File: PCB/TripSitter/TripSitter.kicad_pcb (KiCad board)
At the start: 4 copper layers, 203 x 85 mm, 155 parts, among them IC1 MT25QL256ABA1EW9-0SIT, IC701 IP4220CZ6, J1 Conn_ARM_JTAG_SWD_20, J2 DE15_Plug_HighDensity_Mountin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, J201 Conn_ARM_JTAG_SWD_20, J3 USB_B_Micro, J6 EFM32_PinHeader_PortE, J7 HDMI_A_1.4, J801 Conn_02x05_Odd_Even, J802 Jack-DC, J803 USB_B_Micro, SW1 SW_Push_Open, SW801 SW_DPDT_x2, U1 XC7A100T-FGG484, U2 TPS54325_PWP_14, U201 EFM32GG11B420F2048GQ100, U202 IS62WVS2568FBLL-20NLI, U4 DSC1001DL5-100.0000T, U5 TPS54294PWP, U6 IS62WVS2568FBLL-20NLI, U7 TPD12S520DBT, Y201 48MHz

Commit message: mcu debug edit
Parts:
- removed J1: Conn_ARM_JTAG_SWD_20, Connector_PinHeader_2.54mm:PinHeader_2x07_P2.54mm_Vertical_SMD
- added J4: Conn_02x07_Odd_Even, Connector_PinHeader_2.54mm:PinHeader_2x07_P2.54mm_Vertical_SMD, F.Cu at (209.2, 57.9)
- J201: footprint Connector_PinHeader_1.27mm:PinHeader_2x10_P1.27mm_Vertical_SMD -> Connector_PinHeader_2.54mm:PinHeader_2x10_P2.54mm_Vertical_SMD
- moved J201 27.0 mm to (163.8, 88.5)
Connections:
- D1 pad 1: +5V -> Net-(D1-K)
- R31 pad 1: /FPGA Artix-7 100T 1FGG484C/HDMI Connector/5V_2 -> Net-(D1-K)
- R32 pad 1: /FPGA Artix-7 100T 1FGG484C/HDMI Connector/5V_2 -> Net-(D1-K)
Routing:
- net GND: track 578.0 -> 615.1 mm, vias 239 -> 241
- net Net-(J201-TDI): track 14.8 -> 46.4 mm
- net Net-(J201-TMS/SWDIO): track 12.5 -> 42.9 mm
- net Net-(J201-TCK/SWDCLK): track 11.0 -> 40.5 mm
- net Net-(J201-TDO/SWO): track 11.4 -> 38.5 mm
- net EFM32_RESETN: track 73.1 -> 99.7 mm
- net Net-(D1-K): track 0.00 -> 15.0 mm, vias 0 -> 2
- net Net-(J4-Pin_4): track 31.8 -> 45.8 mm
- net +3.3V: track 100.8 -> 105.9 mm
- net /FPGA Artix-7 100T 1FGG484C/HDMI Connector/5V_2: track 4.47 -> 0.00 mm, vias 2 -> 0
- net Net-(J4-Pin_10): track 30.6 -> 34.4 mm
- net Net-(J4-Pin_6): track 29.5 -> 32.9 mm
- net Net-(J4-Pin_8): track 30.7 -> 32.7 mm
- net +5V: track 269.1 -> 267.5 mm

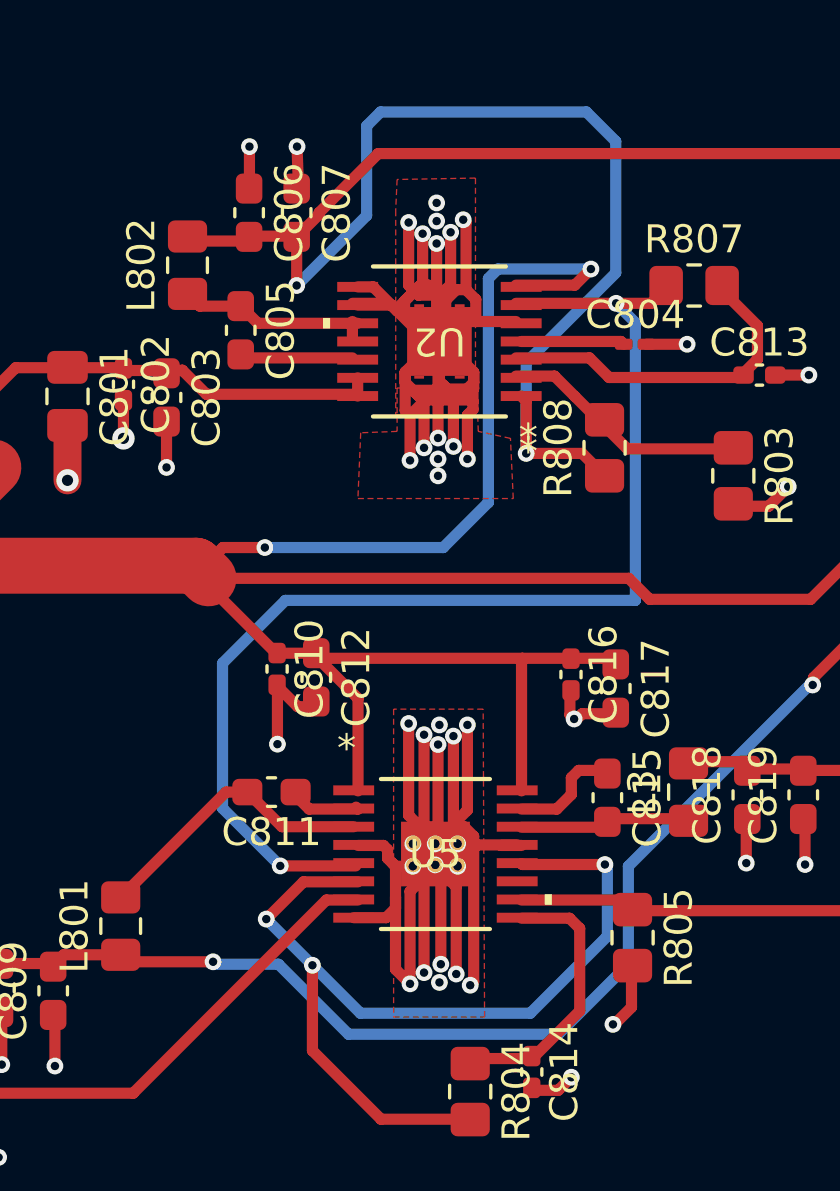
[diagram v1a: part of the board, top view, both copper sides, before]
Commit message: fix heatsink
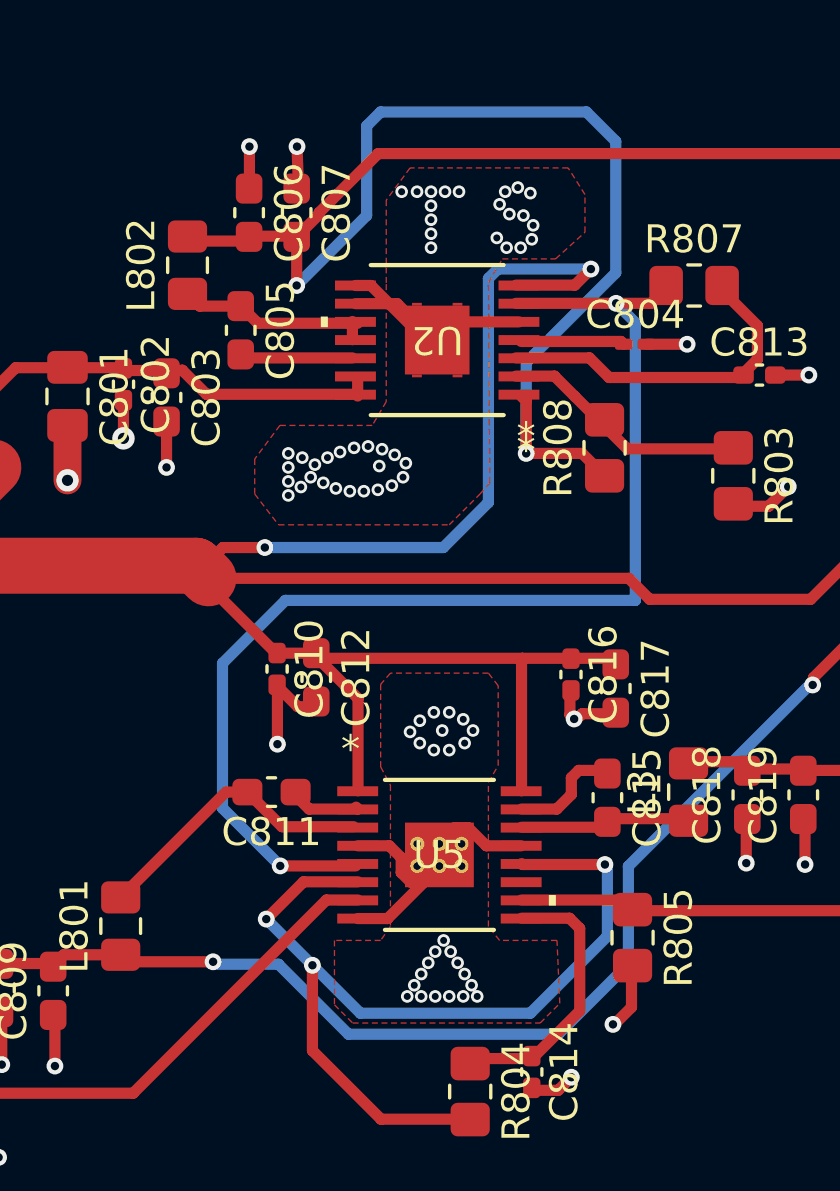
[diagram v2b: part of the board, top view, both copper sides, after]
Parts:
- moved U5 0.15 mm to (63.5, 68.8)
- moved U2 0.09 mm to (63.4, 50.5)
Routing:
- net GND: track 615.1 -> 520.7 mm, vias 241 -> 284

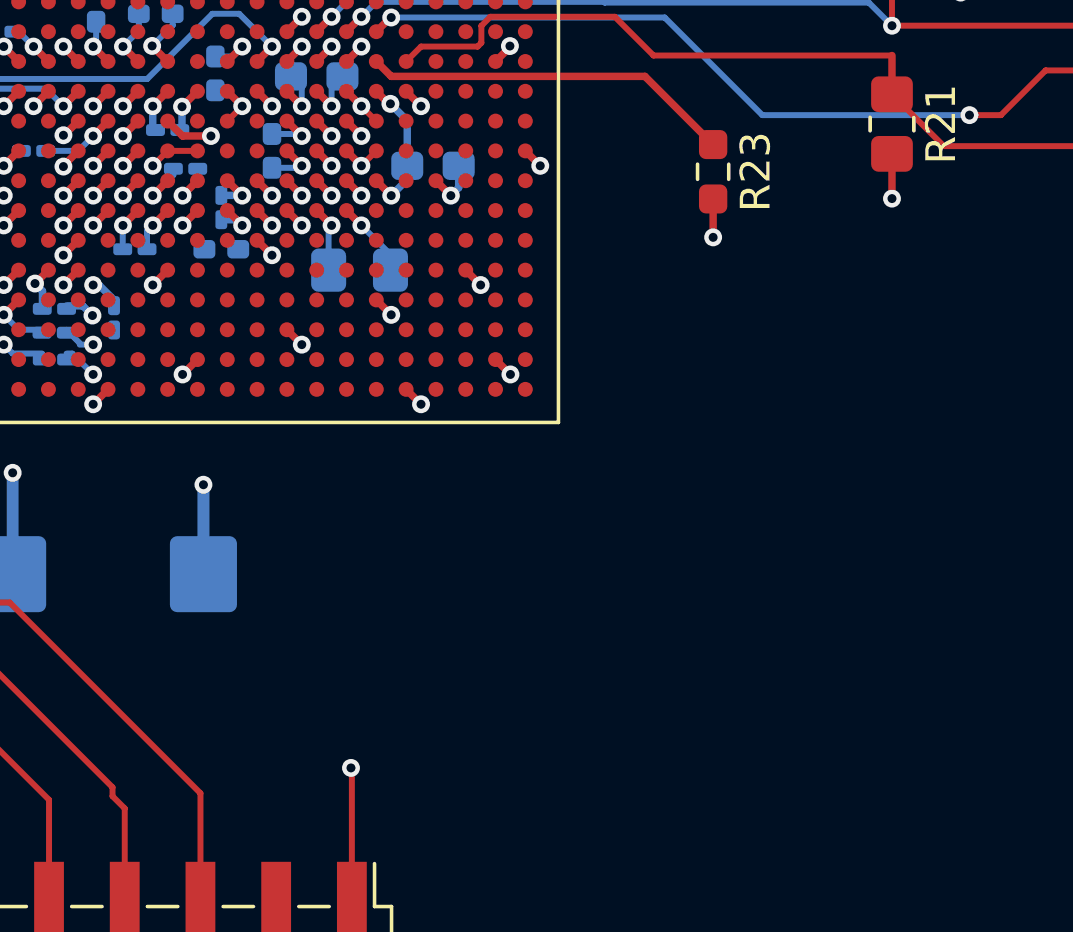
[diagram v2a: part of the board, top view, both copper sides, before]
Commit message: route 2 separate QSPI buses to SRAM from FPGA
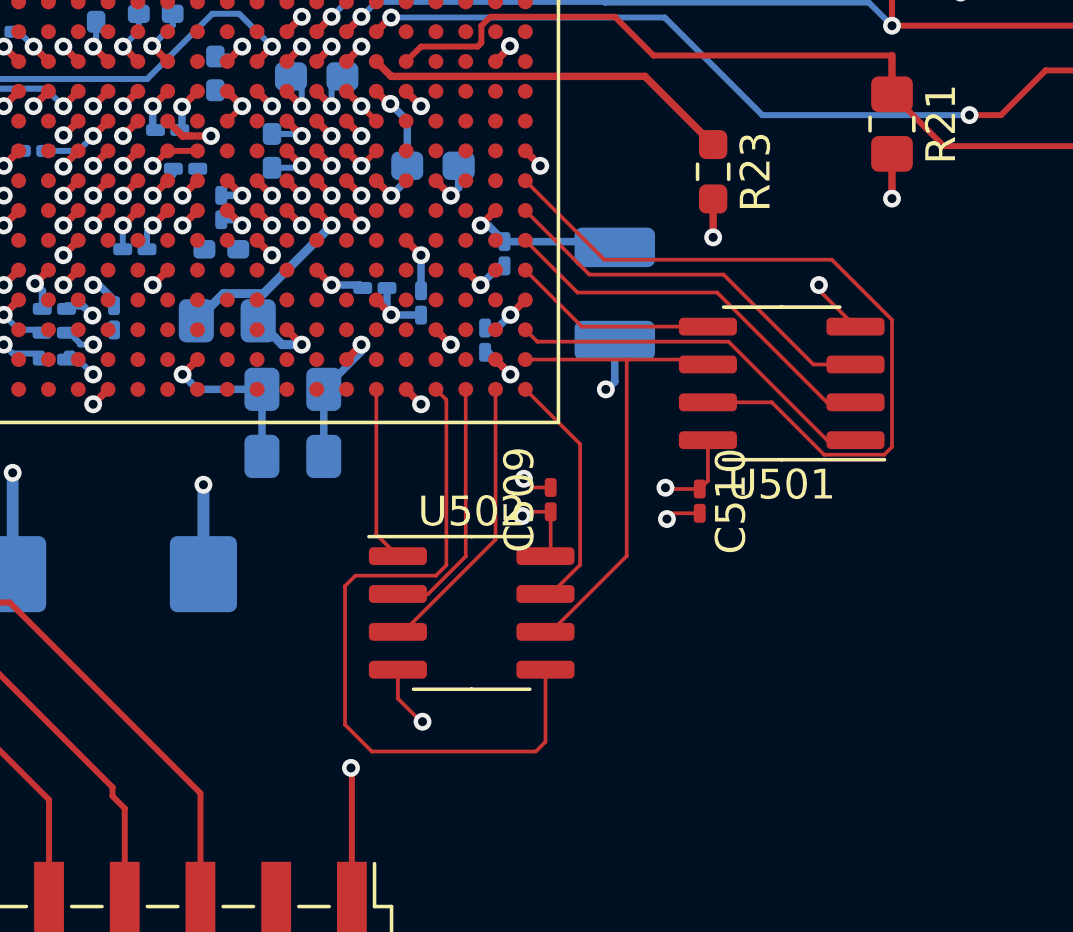
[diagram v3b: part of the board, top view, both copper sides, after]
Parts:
- added C501: 47uF, Capacitor_SMD:C_1210_3225Metric_Pad1.33x2.70mm_HandSolder, B.Cu at (184.1, 65.4)
- added C502: 4.7uF, Capacitor_SMD:C_0805_2012Metric_Pad1.18x1.45mm_HandSolder, B.Cu at (173.3, 68.6)
- added C503: 4.7uF, Capacitor_SMD:C_0805_2012Metric_Pad1.18x1.45mm_HandSolder, B.Cu at (173.3, 70.8)
- added C504: 470nF, Capacitor_SMD:C_0201_0603Metric_Pad0.64x0.40mm_HandSolder, B.Cu at (180.4, 64.0)
- added C506: 470nF, Capacitor_SMD:C_0201_0603Metric_Pad0.64x0.40mm_HandSolder, B.Cu at (177.6, 65.7)
- added C507: 470nF, Capacitor_SMD:C_0201_0603Metric_Pad0.64x0.40mm_HandSolder, B.Cu at (179.8, 67.0)
- added C508: 470nF, Capacitor_SMD:C_0201_0603Metric_Pad0.64x0.40mm_HandSolder, B.Cu at (176.1, 65.2)
- added C509: 0.1uF, Capacitor_SMD:C_0201_0603Metric_Pad0.64x0.40mm_HandSolder, F.Cu at (181.9, 72.3)
- added C510: 0.1uF, Capacitor_SMD:C_0201_0603Metric_Pad0.64x0.40mm_HandSolder, F.Cu at (186.9, 72.3)
- added U501: IS62WVS2568FBLL-20NLI, Package_SO:SOIC-8_3.9x4.9mm_P1.27mm, F.Cu at (189.7, 68.4)
- added U502: IS62WVS2568FBLL-20NLI, Package_SO:SOIC-8_3.9x4.9mm_P1.27mm, F.Cu at (179.3, 76.1)
- moved C33 4.75 mm to (171.1, 66.3)
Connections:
- U1 pad AA1: unconnected-(U1H-IO_L7P_T1_34-PadAA1) -> /FPGA Artix-7 100T 1FGG484C/DDR3/SRAM_QSPI2_DQ2
- U1 pad AA7: unconnected-(U1H-VCCO_34-PadAA7) -> +3.3V
- U1 pad AB1: unconnected-(U1H-IO_L7N_T1_34-PadAB1) -> /FPGA Artix-7 100T 1FGG484C/DDR3/SRAM_QSPI2_DQ3
- U1 pad AB2: unconnected-(U1H-IO_L8N_T1_34-PadAB2) -> /FPGA Artix-7 100T 1FGG484C/DDR3/SRAM_QSPIX_SCLK
- U1 pad AB3: unconnected-(U1H-IO_L8P_T1_34-PadAB3) -> /FPGA Artix-7 100T 1FGG484C/DDR3/SRAM_QSPI1_CS0
- U1 pad AB4: unconnected-(U1H-VCCO_34-PadAB4) -> +3.3V
- U1 pad AB5: unconnected-(U1H-IO_L10N_T1_34-PadAB5) -> /FPGA Artix-7 100T 1FGG484C/DDR3/SRAM_QSPI1_DQ0
- U1 pad AB6: unconnected-(U1H-IO_L20N_T3_34-PadAB6) -> /FPGA Artix-7 100T 1FGG484C/DDR3/SRAM_QSPI1_DQ1
- U1 pad AB7: unconnected-(U1H-IO_L20P_T3_34-PadAB7) -> /FPGA Artix-7 100T 1FGG484C/DDR3/SRAM_QSPI1_DQ2
- U1 pad AB8: unconnected-(U1H-IO_L22N_T3_34-PadAB8) -> /FPGA Artix-7 100T 1FGG484C/DDR3/SRAM_QSPI1_DQ3
- U1 pad R5: unconnected-(U1H-VCCO_34-PadR5) -> +3.3V
- U1 pad T2: unconnected-(U1H-VCCO_34-PadT2) -> +3.3V
- U1 pad U1: unconnected-(U1H-IO_L1N_T0_34-PadU1) -> /FPGA Artix-7 100T 1FGG484C/DDR3/SRAM_QSPI2_CS0
- U1 pad V6: unconnected-(U1H-VCCO_34-PadV6) -> +3.3V
- U1 pad W1: unconnected-(U1H-IO_L5P_T0_34-PadW1) -> /FPGA Artix-7 100T 1FGG484C/DDR3/SRAM_QSPI2_DQ0
- U1 pad W3: unconnected-(U1H-VCCO_34-PadW3) -> +3.3V
- U1 pad Y1: unconnected-(U1H-IO_L5N_T0_34-PadY1) -> /FPGA Artix-7 100T 1FGG484C/DDR3/SRAM_QSPI2_DQ1
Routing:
- net /FPGA Artix-7 100T 1FGG484C/DDR3/SRAM_QSPI1_DQ3: track 0.00 -> 25.5 mm
- net /FPGA Artix-7 100T 1FGG484C/DDR3/SRAM_QSPI2_DQ0: track 0.00 -> 24.0 mm
- net +3.3V: track 105.9 -> 128.4 mm, vias 55 -> 63
- net GND: track 520.7 -> 538.2 mm, vias 284 -> 289
- net /FPGA Artix-7 100T 1FGG484C/DDR3/SRAM_QSPIX_SCLK: track 0.00 -> 16.6 mm
- net /FPGA Artix-7 100T 1FGG484C/DDR3/SRAM_QSPI1_DQ1: track 0.00 -> 13.3 mm
- net /FPGA Artix-7 100T 1FGG484C/DDR3/SRAM_QSPI1_DQ2: track 0.00 -> 13.2 mm
- net /FPGA Artix-7 100T 1FGG484C/DDR3/SRAM_QSPI1_CS0: track 0.00 -> 12.6 mm
- net /FPGA Artix-7 100T 1FGG484C/DDR3/SRAM_QSPI2_DQ2: track 0.00 -> 9.60 mm
- net /FPGA Artix-7 100T 1FGG484C/DDR3/SRAM_QSPI2_DQ1: track 0.00 -> 8.40 mm
- net /FPGA Artix-7 100T 1FGG484C/DDR3/SRAM_QSPI2_DQ3: track 0.00 -> 8.21 mm
- net /FPGA Artix-7 100T 1FGG484C/DDR3/SRAM_QSPI1_DQ0: track 0.00 -> 6.91 mm
- net /FPGA Artix-7 100T 1FGG484C/DDR3/SRAM_QSPI2_CS0: track 0.00 -> 5.90 mm
- net +1V0: track 216.0 -> 220.5 mm

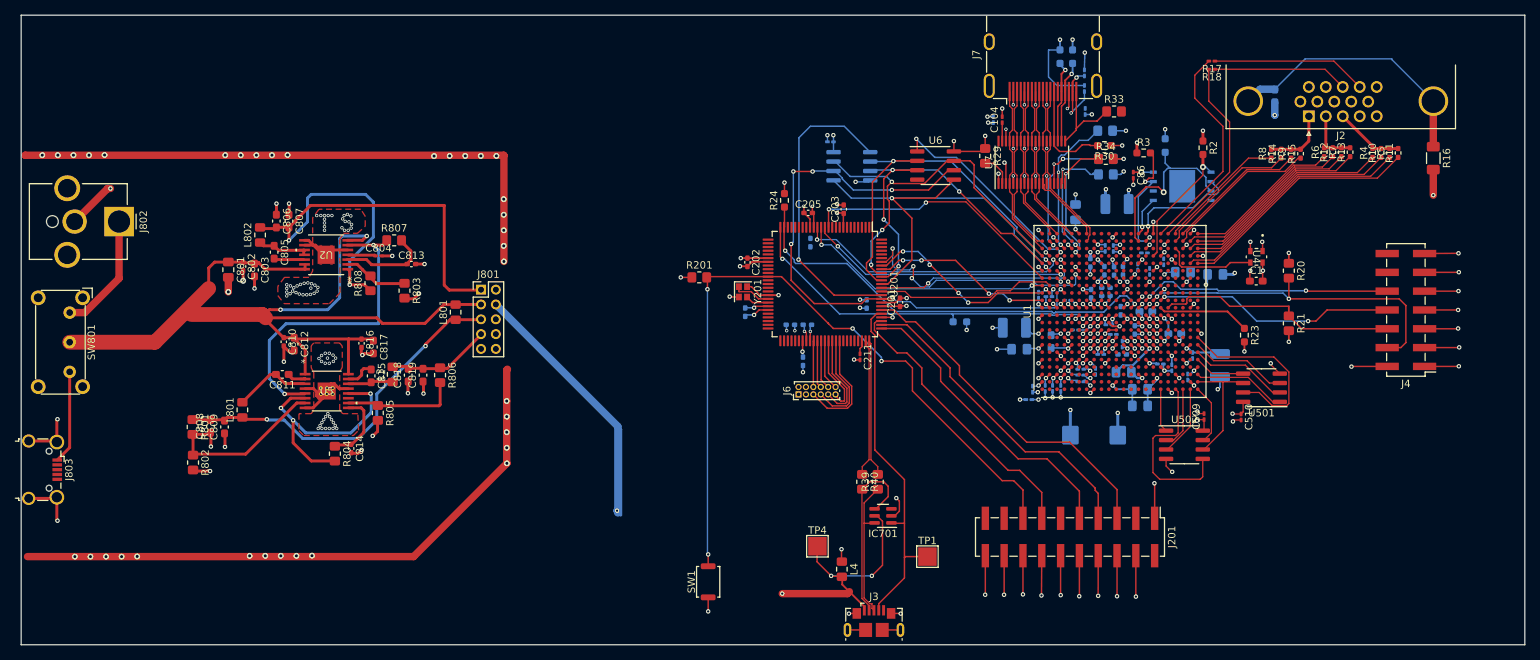
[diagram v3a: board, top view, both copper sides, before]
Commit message: Fix DRC errors + silkscreen and make logo
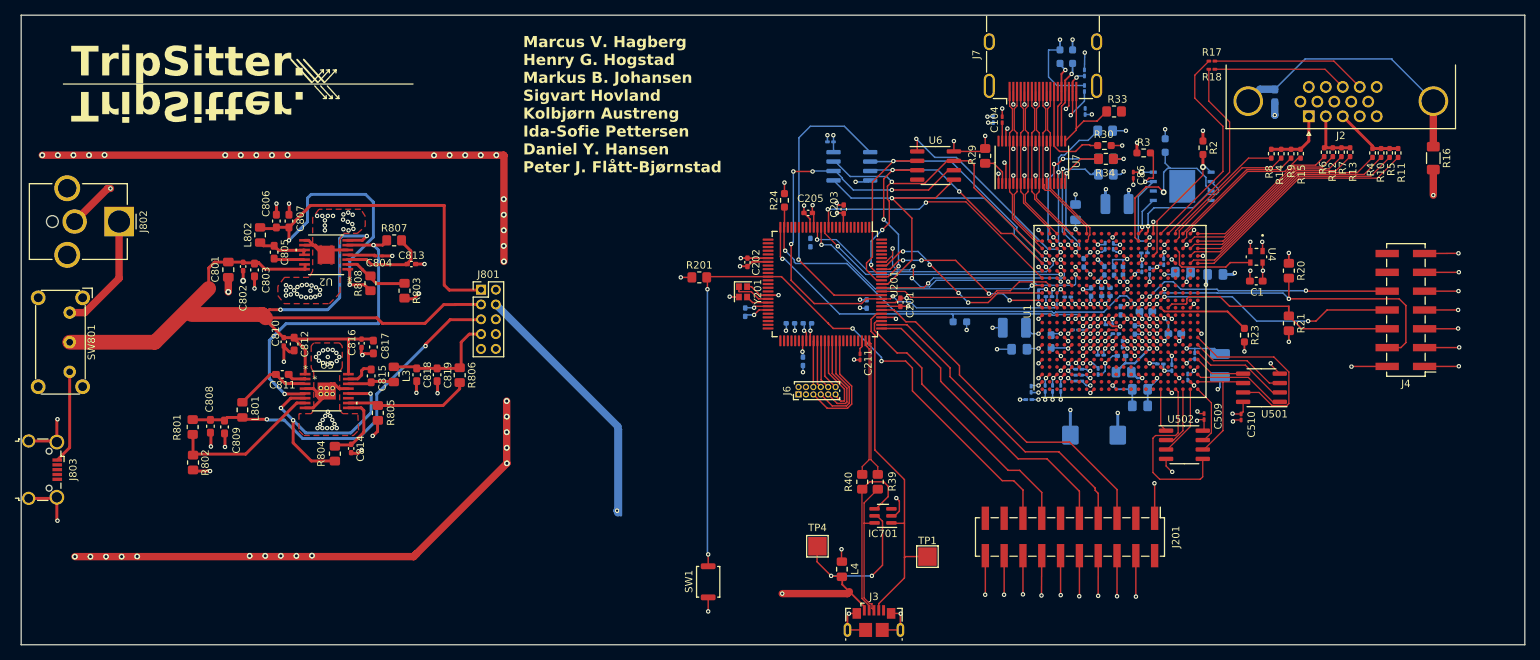
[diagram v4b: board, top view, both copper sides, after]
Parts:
- removed the L801 at (80.9, 58.2)
- moved R806 2.65 mm to (81.5, 66.7)
- moved C819 1.90 mm to (78.4, 66.7)
- moved C818 1.15 mm to (75.7, 66.7)
- moved C29 0.90 mm to (165.7, 51.5)
- moved C81 0.60 mm to (173.6, 52.4)
- moved C101 0.45 mm to (163.6, 56.1)
- moved C56 0.36 mm to (170.1, 61.1)
- moved C53 0.35 mm to (167.7, 66.2)
- moved C504 0.31 mm to (180.7, 64.1)
- moved C42 0.30 mm to (169.7, 49.3)
- moved C43 0.30 mm to (168.6, 49.3)
- moved C51 0.27 mm to (165.1, 67.5)
- moved C49 0.25 mm to (165.1, 65.9)
- moved C52 0.25 mm to (165.0, 66.7)
- moved C14 0.23 mm to (166.7, 55.5)
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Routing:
- net +3.3V: track 128.4 -> 134.4 mm
- net GND: track 538.2 -> 542.5 mm, vias 289 -> 279
- net +1V0: track 220.5 -> 224.0 mm
- net Net-(U5-VFB2): track 15.5 -> 17.0 mm
- net /PCB Power System/3V3: track 14.2 -> 15.7 mm
- net /MCU EFM32GG11B420/VBUS: track 39.1 -> 40.1 mm
- net +5V: track 267.5 -> 268.5 mm
- net +1V8: track 124.2 -> 125.1 mm
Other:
- board text added: "Marcus V. Hagberg Henry G. Hogstad Markus B. Johansen Sigvart Hovland Kolbjørn Austreng Ida-Sofie Pettersen Daniel Y. Hansen Peter J. Flått-Bjørnstad"
- board text added: "TripSitter."
